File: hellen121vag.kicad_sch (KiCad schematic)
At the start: 31 parts, among them J21 Conn_01x05_Male, J22 USB_B_Mini, M1 Module-power_12and5V-0.3, M2 Module-knock-0.2, M3 Module-vr-discrete-0.5, M4 Module-vr-max9924-0.1, M5 Module-wbo-0.5, M6 Module:mega-mcu100/0.3, M7 Module-can-0.1, M8 Module-motor-driver-0.1, P1 368255-2, U10 BTS6143D

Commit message: se hace un test de la modificacion
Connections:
- net DC1_DIS is gone; now on net DC1_DIS_W1: M6.E8 (SPI2_MISO_(PB14))
- net DC1_DIR: now also M8.W4 (DIR)
- net DC1_PWM: now also M8.W2 (PWM)
- net DC1_DIS_W1: now reaches M8.W1 (DIS)
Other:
- removed sheet DC Driver 1
- moved on the sheet: U10
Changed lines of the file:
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@@
 	(wire
 		(pts
+			(xy 279.4 196.85) (xy 279.4 177.8)
+		)
+		(stroke
+			(width 0)
+			(type default)
+		)
+	)
+	(wire
+		(pts
 			(xy 298.45 156.21) (xy 298.45 161.29)
 		)
@@
 	(wire
 		(pts
+			(xy 252.73 196.85) (xy 279.4 196.85)
+		)
+		(stroke
+			(width 0)
+			(type default)
+		)
+	)
+	(wire
+		(pts
 			(xy 300.99 106.68) (xy 300.99 118.11)
 		)
@@
 	(wire
 		(pts
+			(xy 279.4 177.8) (xy 281.94 177.8)
+		)
+		(stroke
+			(width 0)
+			(type default)
+		)
+	)
+	(wire
+		(pts
 			(xy 276.86 104.14) (xy 303.53 104.14)
 		)
@@
 	(wire
 		(pts
-			(xy 276.86 182.88) (xy 284.48 182.88)
-		)
-		(stroke
-			(width 0)
-			(type default)
-		)
-	)
-	(wire
-		(pts
 			(xy 275.59 260.35) (xy 275.59 273.05)
 		)
@@
 	(wire
 		(pts
-			(xy 276.86 177.8) (xy 281.94 177.8)
-		)
-		(stroke
-			(width 0)
-			(type default)
-		)
-	)
-	(wire
-		(pts
 			(xy 294.64 209.55) (xy 303.53 209.55)
 		)
@@
 	(wire
 		(pts
-			(xy 276.86 198.12) (xy 285.75 198.12)
-		)
-		(stroke
-			(width 0)
-			(type default)
-		)
-	)
-	(wire
-		(pts
 			(xy 153.67 180.34) (xy 153.67 177.8)
 		)
@@
 	(wire
 		(pts
+			(xy 252.73 194.31) (xy 259.08 194.31)
+		)
+		(stroke
+			(width 0)
+			(type default)
+		)
+	)
+	(wire
+		(pts
 			(xy 186.69 260.35) (xy 190.5 260.35)
 		)
@@
 	(wire
 		(pts
-			(xy 285.75 198.12) (xy 285.75 176.53)
-		)
-		(stroke
-			(width 0)
-			(type default)
-		)
-	)
-	(wire
-		(pts
 			(xy 288.29 179.07) (xy 303.53 179.07)
 		)
@@
 	(wire
 		(pts
+			(xy 259.08 194.31) (xy 259.08 189.23)
+		)
+		(stroke
+			(width 0)
+			(type default)
+		)
+	)
+	(wire
+		(pts
 			(xy 149.86 180.34) (xy 153.67 180.34)
 		)
@@
 		)
 	)
-	(wire
-		(pts
-			(xy 276.86 203.2) (xy 285.75 203.2)
-		)
-		(stroke
-			(width 0)
-			(type default)
-		)
-	)
 	(bus
 		(pts
@@
 	(wire
 		(pts
-			(xy 276.86 180.34) (xy 284.48 180.34)
+			(xy 252.73 143.51) (xy 241.3 143.51)
 		)
 		(stroke
@@
 	(wire
 		(pts
-			(xy 252.73 143.51) (xy 241.3 143.51)
+			(xy 176.53 194.31) (xy 176.53 195.58)
 		)
 		(stroke
@@
 	(wire
 		(pts
-			(xy 176.53 194.31) (xy 176.53 195.58)
+			(xy 252.73 199.39) (xy 284.48 199.39)
 		)
 		(stroke
@@
 	(wire
 		(pts
-			(xy 284.48 180.34) (xy 284.48 173.99)
+			(xy 284.48 173.99) (xy 284.48 199.39)
 		)
 		(stroke
@@
 	(wire
 		(pts
-			(xy 276.86 200.66) (xy 285.75 200.66)
-		)
-		(stroke
-			(width 0)
-			(type default)
-		)
-	)
-	(wire
-		(pts
 			(xy 241.3 166.37) (xy 259.08 166.37)
 		)
@@
 		)
 	)
-	(label "DC2_DIS"
-		(at 276.86 203.2 0)
-		(effects
-			(font
-				(size 1.27 1.27)
-			)
-			(justify left bottom)
-		)
-	)
 	(label "3_WBO_Heater"
 		(at 163.83 60.96 0)
@@
 		)
 	)
-	(label "DC1_DIS"
-		(at 276.86 182.88 0)
-		(effects
-			(font
-				(size 1.27 1.27)
-			)
-			(justify left bottom)
-		)
-	)
 	(label "PWR_EN"
 		(at 290.83 270.51 0)
@@
 		)
 	)
-	(label "DC2_PWM"
-		(at 276.86 198.12 0)
-		(effects
-			(font
-				(size 1.27 1.27)
-			)
-			(justify left bottom)
-		)
-	)
 	(label "VR_MAX9924"
 		(at 372.11 171.45 0)
@@
 		)
 	)
-	(label "DC2_DIR"
-		(at 276.86 200.66 0)
-		(effects
-			(font
-				(size 1.27 1.27)
-			)
-			(justify left bottom)
-		)
-	)
 	(label "MISO3"
 		(at 372.11 135.89 0)
@@
 		)
 	)
+	(global_label "DC1_DIS_W1"
+		(shape input)
+		(at 259.08 189.23 0)
+		(fields_autoplaced yes)
+		(effects
+			(font
+				(size 1.27 1.27)
+			)
+			(justify left)
+		)
+		(property "Intersheetrefs" "${INTERSHEET_REFS}"
+			(at 273.5902 189.23 0)
+			(effects
+				(font
+					(size 1.27 1.27)
+				)
+				(justify left)
+				(hide yes)
+			)
+		)
+	)
 	(global_label "PIN27"
 		(shape input)
@@
 		)
 	)
+	(global_label "DC1_DIS_W1"
+		(shape input)
+		(at 381 118.11 0)
+		(fields_autoplaced yes)
+		(effects
+			(font
+				(size 1.27 1.27)
+			)
+			(justify left)
+		)
+		(property "Intersheetrefs" "${INTERSHEET_REFS}"
+			(at 395.5102 118.11 0)
+			(effects
+				(font
+					(size 1.27 1.27)
+				)
+				(justify left)
+				(hide yes)
+			)
+		)
+	)
 	(global_label "PIN26"
 		(shape input)
@@
 	(symbol
 		(lib_id "Power_Management:BTS6143D")
-		(at 436.88 247.65 0)
+		(at 414.02 210.82 0)
 		(unit 1)
 		(exclude_from_sim no)
@@
 		(fields_autoplaced yes)
 		(property "Reference" "U10"
-			(at 436.88 255.27 0)
+			(at 414.02 218.44 0)
 			(effects
 				(font
@@
 		)
 		(property "Value" "BTS6143D"
-			(at 436.88 257.81 0)
+			(at 414.02 220.98 0)
 			(effects
 				(font
@@
 		)
 		(property "Footprint" "Package_TO_SOT_SMD:TO-252-4"
-			(at 436.88 254 0)
+			(at 414.02 217.17 0)
 			(effects
 				(font
@@
 		)
 		(property "Datasheet" "http://www.infineon.com/dgdl/Infineon-BTS6143D-DS-v01_00-EN.pdf?fileId=5546d4625a888733015aa3da10821022"
-			(at 436.88 257.81 0)
+			(at 414.02 220.98 0)
 			(effects
 				(font
@@
 		)
 		(property "Description" "Smart High-Side Power Switch, PROFET, Single, 10mOhm, 8A, 38V, TO252-5"
-			(at 436.88 247.65 0)
+			(at 414.02 210.82 0)
 			(effects
 				(font
@@
 				)
 			)
-		)
-	)
-	(sheet
-		(at 259.08 175.26)
-		(size 17.78 19.05)
-		(stroke
-			(width 0.1524)
-			(type solid)
-		)
-		(fill
-			(color 0 0 0 0.0000)
-		)
-		(property "Sheetname" "DC Driver 1"
-			(at 269.24 187.325 90)
-			(effects
-				(font
-					(size 1.27 1.27)
-				)
-				(justify left bottom)
-			)
-		)
-		(property "Sheetfile" "DC_MOTOR_0.1.kicad_sch"
-			(at 259.08 188.5446 0)
-			(effects
-				(font
-					(size 1.27 1.27)
-				)
-				(justify left top)
-				(hide yes)
-			)
-		)
-		(pin "OUT+" output
-			(at 259.08 180.34 180)
-			(effects
-				(font
-					(size 1.27 1.27)
-				)
-				(justify left)
-			)
-		)
-		(pin "OUT-" output
-			(at 259.08 182.88 180)
-			(effects
-				(font
-					(size 1.27 1.27)
-				)
-				(justify left)
-			)
-		)
-		(pin "PWR" passive
-			(at 259.08 177.8 180)
-			(effects
-				(font
-					(size 1.27 1.27)
-				)
-				(justify left)
-			)
-		)
-		(pin "PWM" input
-			(at 276.86 177.8 0)
-			(effects
-				(font
-					(size 1.27 1.27)
-				)
-				(justify right)
-			)
-		)
-		(pin "DIR" input
-			(at 276.86 180.34 0)
-			(effects
-				(font
-					(size 1.27 1.27)
-				)
-				(justify right)
-			)
-		)
-		(pin "DIS" input
-			(at 276.86 182.88 0)
-			(effects
-				(font
-					(size 1.27 1.27)
-				)
-				(justify right)
-			)
-		)
-		(pin "3V3" passive
-			(at 259.08 185.42 180)
-			(effects
-				(font
-					(size 1.27 1.27)
-				)
-				(justify left)
-			)
-		)
-		(instances
-			(project "hellen121vag"
-				(path "/45c1f041-3b7c-4036-abe9-e26621c05a73"
-					(page "2")
-				)
-			)

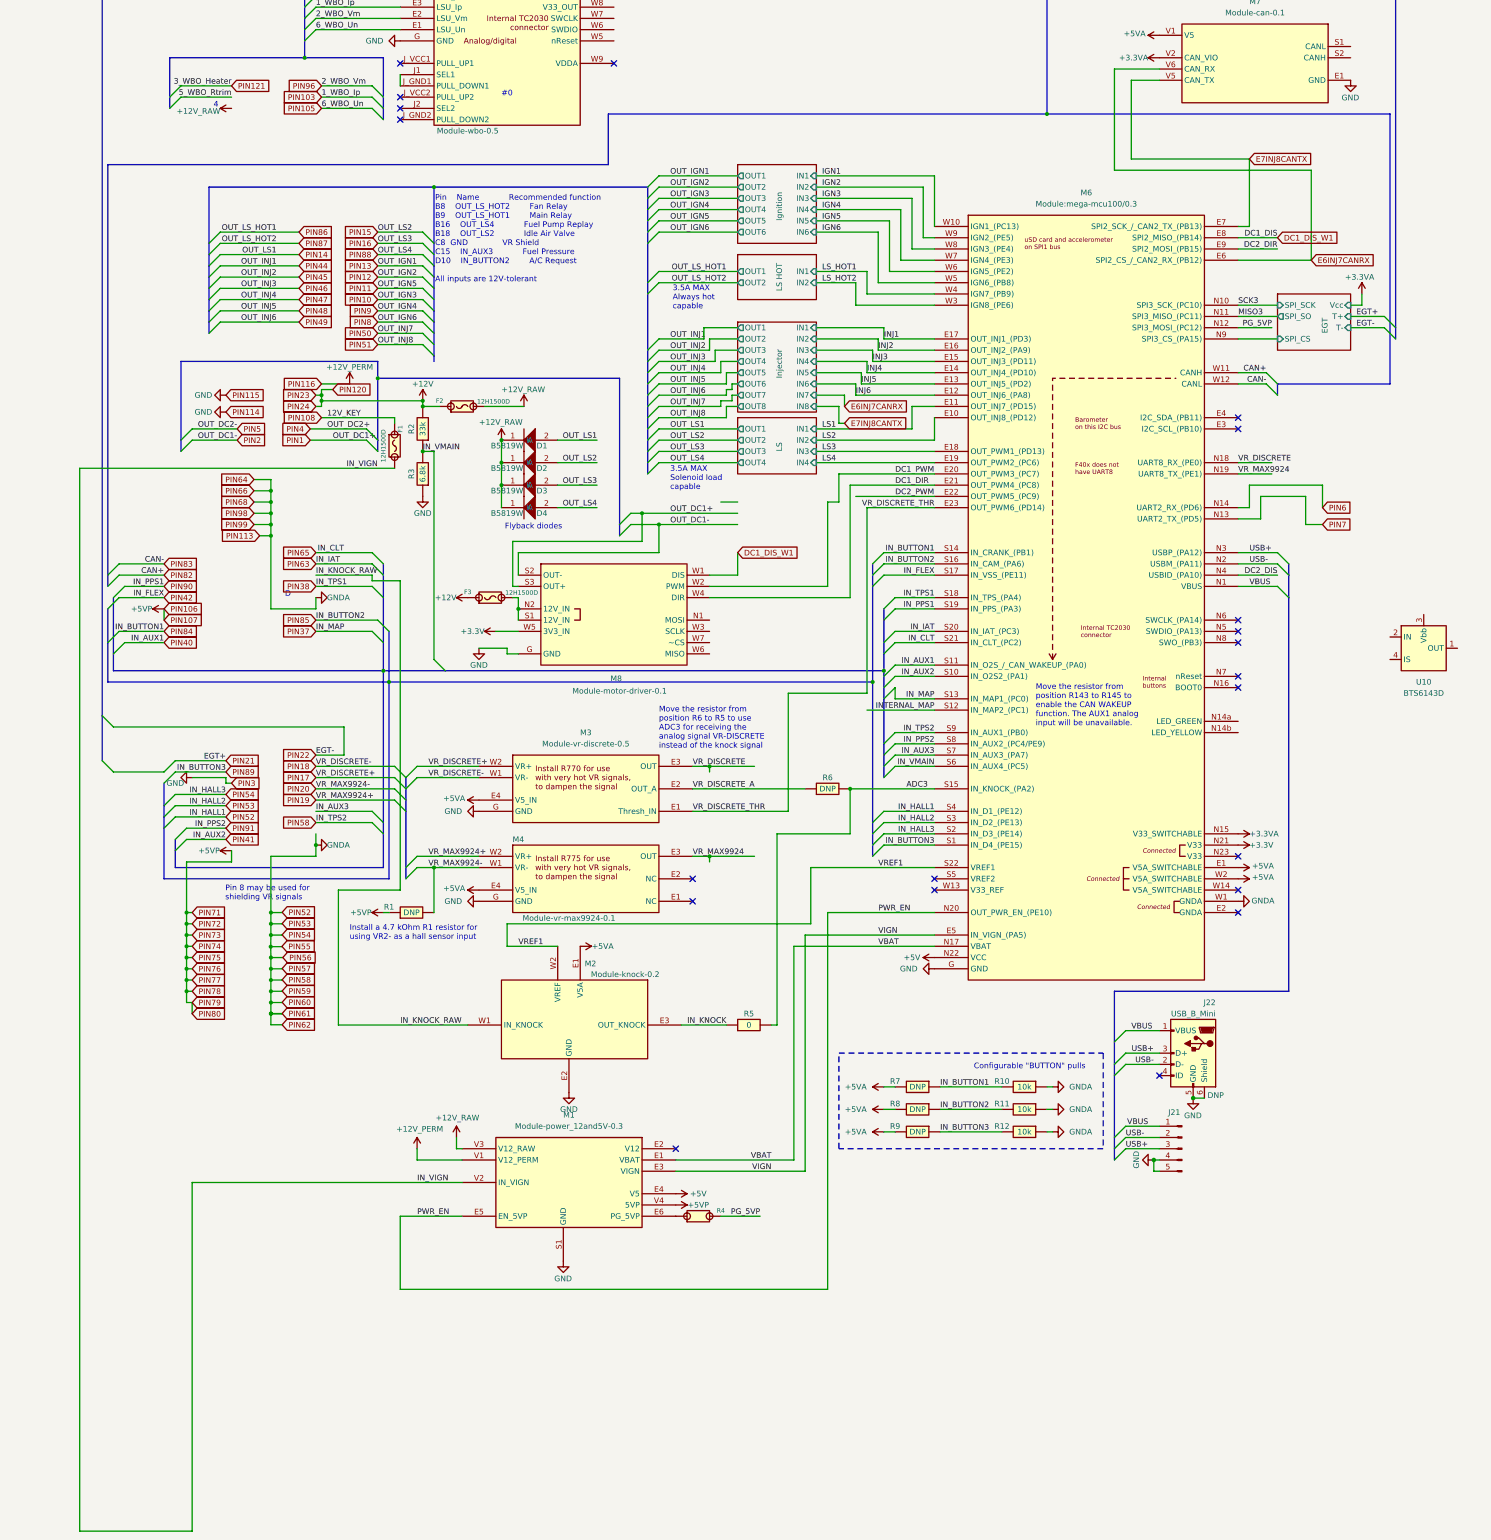
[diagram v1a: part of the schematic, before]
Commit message: colocacion de componentes 100%
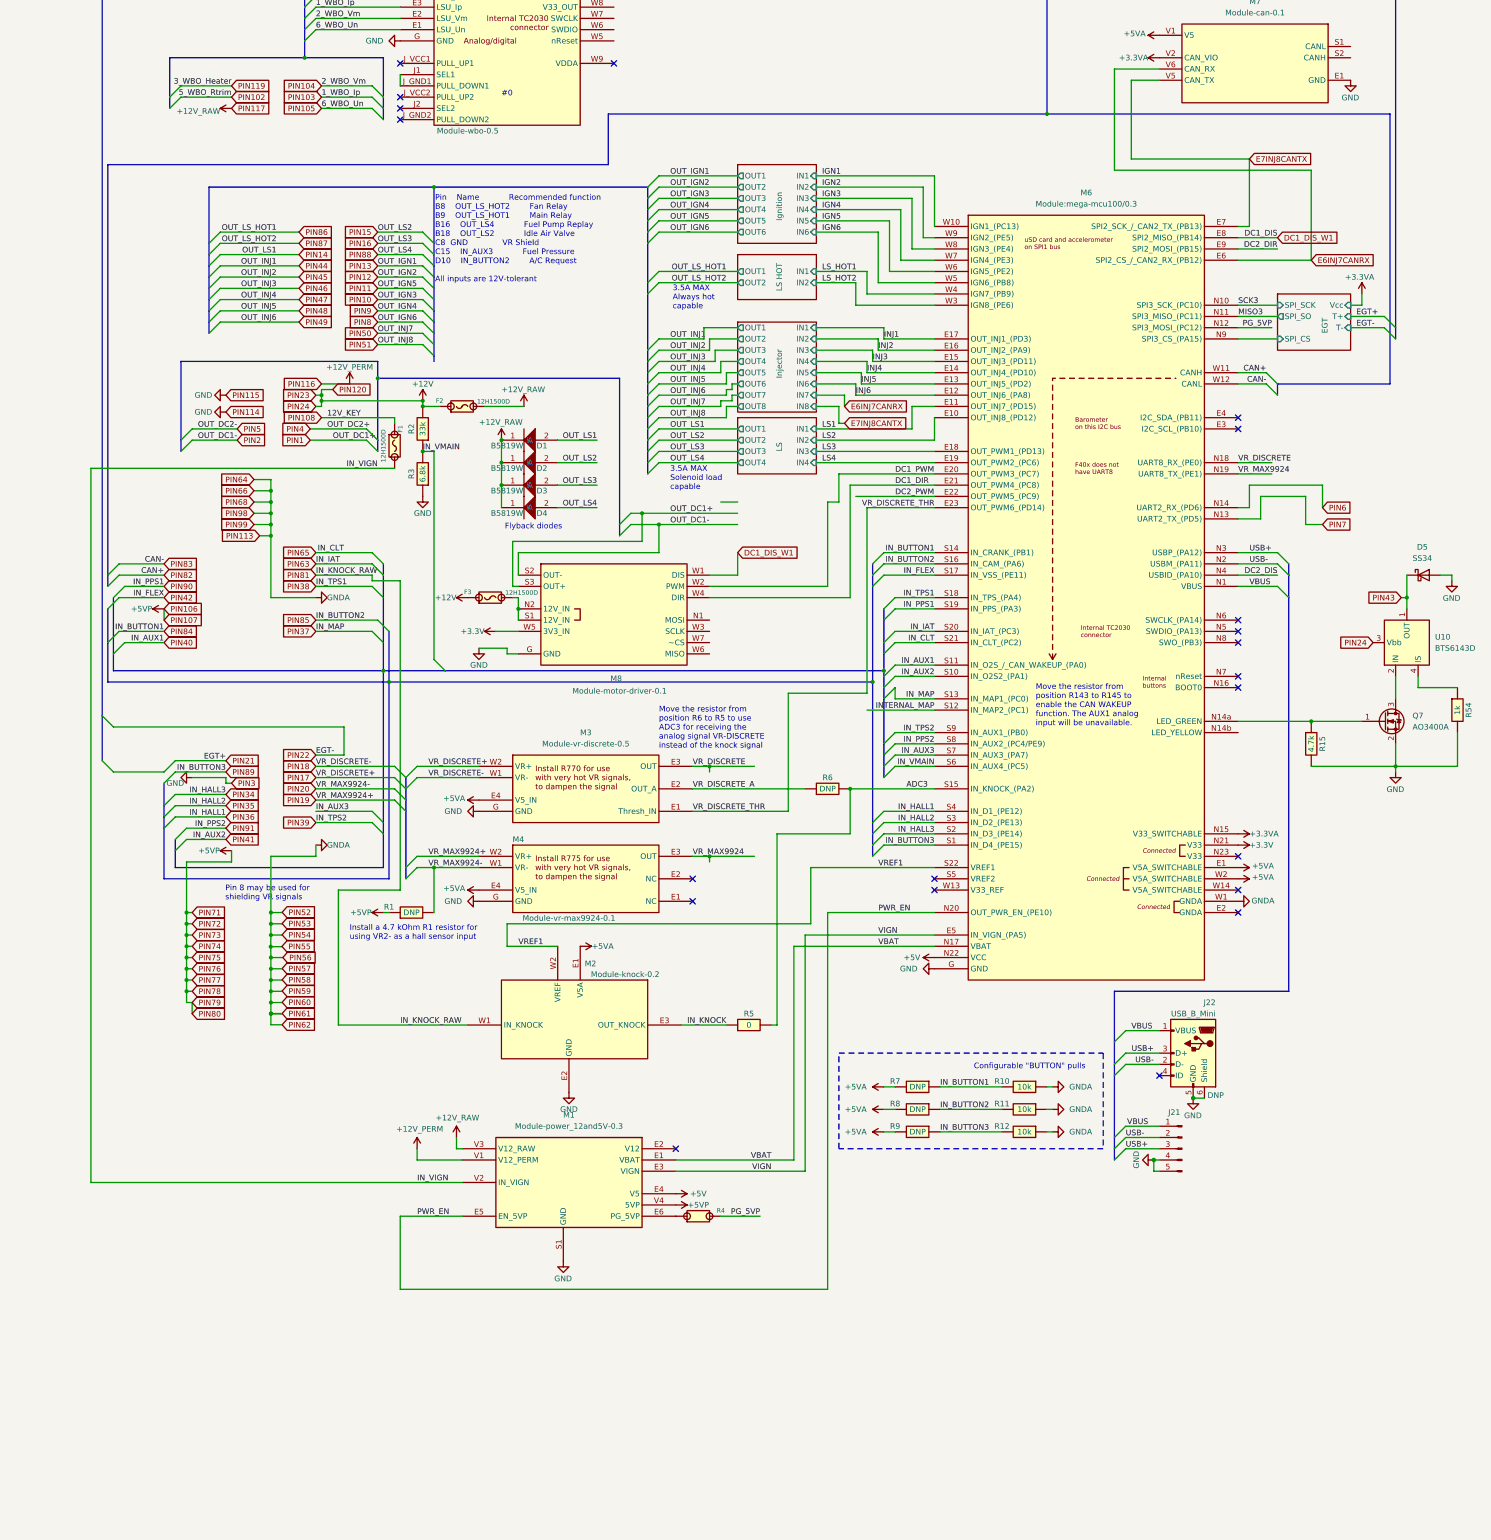
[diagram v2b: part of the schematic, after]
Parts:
- added D5: SS34, Diode_SMD:D_SMA, symbol Diode:SS34
- added Q7: AO3400A, Package_TO_SOT_SMD:SOT-23, symbol Transistor_FET:AO3400A
- added R15: 4.7k, hellen-one-common:R0603, symbol hellen-one-common:Res
- added R54: 1k, hellen-one-common:R0603, symbol hellen-one-common:Res
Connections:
- net 5_WBO_Rtrim is gone; now on net PIN102: M5.E4 (LSU_Rtrim)
- net IN_KNOCK_RAW is gone; now on net PIN81: M2.W1 (IN_KNOCK)
- net PIN117 is gone; now on net +12V_RAW: P1.117
- net +12V: now also U10.3 (Vbb)
- net GND: now also D5.2 (A), Q7.2 (S), R15.2, R54.2
- net GNDA: no longer M6.S2 (IN_D3_(PE14)), M6.S3 (IN_D2_(PE13)), M6.S4 (IN_D1_(PE12)), M6.S9 (IN_AUX1_(PB0))
- net PIN104: now also M5.E2 (LSU_Vm)
- net PIN119: now also M5.E5 (LSU_H+)
- net PIN121: no longer M5.E5 (LSU_H+)
- net PIN34: now also M6.S2 (IN_D3_(PE14))
- net PIN35: now also M6.S3 (IN_D2_(PE13))
- net PIN36: now also M6.S4 (IN_D1_(PE12))
- net PIN39: now also M6.S9 (IN_AUX1_(PB0))
- net PIN43: now also U10.1 (OUT), U10.5 (OUT), D5.1 (K)
- net PIN96: no longer M5.E2 (LSU_Vm)
- net at U10.2 (IN): now also Q7.3 (D)
- net at U10.4 (IS): now also R54.1
- net at M6.N14a (LED_GREEN): now also Q7.1 (G), R15.1
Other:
- note removed: "4"
- note removed: "D"
- moved on the sheet: U10
